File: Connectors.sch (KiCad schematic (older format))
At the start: 4 parts

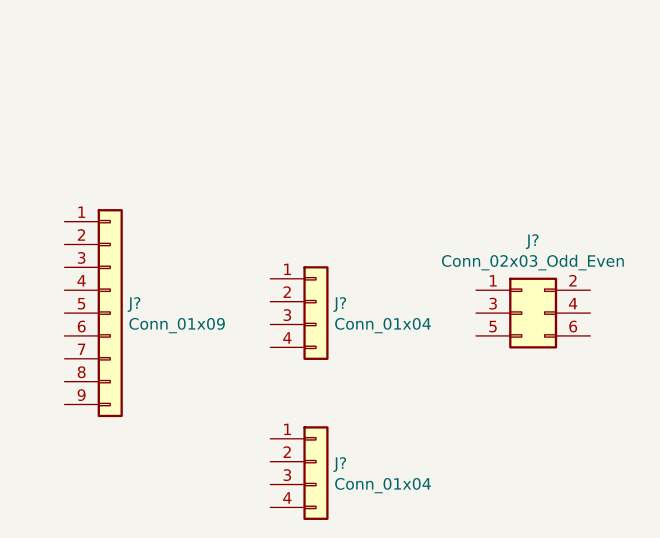
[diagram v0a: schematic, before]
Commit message: Símbolos organizados
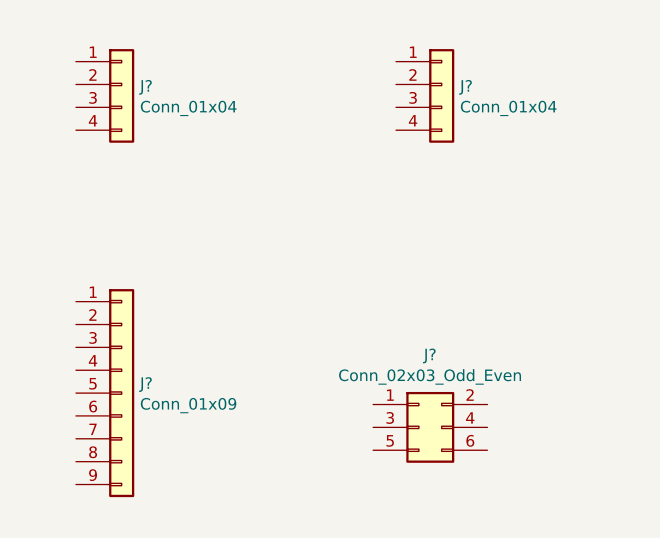
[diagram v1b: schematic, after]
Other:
- moved on the sheet: J?
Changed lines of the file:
@@
 L Connector_Generic:Conn_01x09 J?
 U 1 1 5F03BAF3
-P 5050 3000
-F 0 "J?" H 5130 3042 50  0000 L CNN
-F 1 "Conn_01x09" H 5130 2951 50  0000 L CNN
-F 2 "" H 5050 3000 50  0001 C CNN
-F 3 "~" H 5050 3000 50  0001 C CNN
-	1    5050 3000
+P 5100 3350
+F 0 "J?" H 5180 3392 50  0000 L CNN
+F 1 "Conn_01x09" H 5180 3301 50  0000 L CNN
+F 2 "" H 5100 3350 50  0001 C CNN
+F 3 "~" H 5100 3350 50  0001 C CNN
+	1    5100 3350
 	1    0    0    -1
 $EndComp
@@
 L Connector_Generic:Conn_01x04 J?
 U 1 1 5F03C469
-P 5950 2950
-F 0 "J?" H 6030 2942 50  0000 L CNN
-F 1 "Conn_01x04" H 6030 2851 50  0000 L CNN
-F 2 "" H 5950 2950 50  0001 C CNN
-F 3 "~" H 5950 2950 50  0001 C CNN
-	1    5950 2950
+P 5100 2000
+F 0 "J?" H 5180 1992 50  0000 L CNN
+F 1 "Conn_01x04" H 5180 1901 50  0000 L CNN
+F 2 "" H 5100 2000 50  0001 C CNN
+F 3 "~" H 5100 2000 50  0001 C CNN
+	1    5100 2000
 	1    0    0    -1
 $EndComp
@@
 L Connector_Generic:Conn_02x03_Odd_Even J?
 U 1 1 5F03D0B3
-P 6850 3000
-F 0 "J?" H 6900 3317 50  0000 C CNN
-F 1 "Conn_02x03_Odd_Even" H 6900 3226 50  0000 C CNN
-F 2 "" H 6850 3000 50  0001 C CNN
-F 3 "~" H 6850 3000 50  0001 C CNN
-	1    6850 3000
+P 6400 3500
+F 0 "J?" H 6450 3817 50  0000 C CNN
+F 1 "Conn_02x03_Odd_Even" H 6450 3726 50  0000 C CNN
+F 2 "" H 6400 3500 50  0001 C CNN
+F 3 "~" H 6400 3500 50  0001 C CNN
+	1    6400 3500
 	1    0    0    -1
 $EndComp
@@
 L Connector_Generic:Conn_01x04 J?
 U 1 1 5F03D928
-P 5950 3650
-F 0 "J?" H 6030 3642 50  0000 L CNN
-F 1 "Conn_01x04" H 6030 3551 50  0000 L CNN
-F 2 "" H 5950 3650 50  0001 C CNN
-F 3 "~" H 5950 3650 50  0001 C CNN
-	1    5950 3650
+P 6500 2000
+F 0 "J?" H 6580 1992 50  0000 L CNN
+F 1 "Conn_01x04" H 6580 1901 50  0000 L CNN
+F 2 "" H 6500 2000 50  0001 C CNN
+F 3 "~" H 6500 2000 50  0001 C CNN
+	1    6500 2000
 	1    0    0    -1
 $EndComp

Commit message: Símbolos anotados
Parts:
- gave numbers to parts that had none: 4
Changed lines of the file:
@@
 $EndDescr
 $Comp
-L Connector_Generic:Conn_01x09 J?
+L Connector_Generic:Conn_01x09 J2
 U 1 1 5F03BAF3
 P 5100 3350
-F 0 "J?" H 5180 3392 50  0000 L CNN
+F 0 "J2" H 5180 3392 50  0000 L CNN
 F 1 "Conn_01x09" H 5180 3301 50  0000 L CNN
 F 2 "" H 5100 3350 50  0001 C CNN
@@
 $EndComp
 $Comp
-L Connector_Generic:Conn_01x04 J?
+L Connector_Generic:Conn_01x04 J1
 U 1 1 5F03C469
 P 5100 2000
-F 0 "J?" H 5180 1992 50  0000 L CNN
+F 0 "J1" H 5180 1992 50  0000 L CNN
 F 1 "Conn_01x04" H 5180 1901 50  0000 L CNN
 F 2 "" H 5100 2000 50  0001 C CNN
@@
 $EndComp
 $Comp
-L Connector_Generic:Conn_02x03_Odd_Even J?
+L Connector_Generic:Conn_02x03_Odd_Even J3
 U 1 1 5F03D0B3
 P 6400 3500
-F 0 "J?" H 6450 3817 50  0000 C CNN
+F 0 "J3" H 6450 3817 50  0000 C CNN
 F 1 "Conn_02x03_Odd_Even" H 6450 3726 50  0000 C CNN
 F 2 "" H 6400 3500 50  0001 C CNN
@@
 $EndComp
 $Comp
-L Connector_Generic:Conn_01x04 J?
+L Connector_Generic:Conn_01x04 J4
 U 1 1 5F03D928
 P 6500 2000
-F 0 "J?" H 6580 1992 50  0000 L CNN
+F 0 "J4" H 6580 1992 50  0000 L CNN
 F 1 "Conn_01x04" H 6580 1901 50  0000 L CNN
 F 2 "" H 6500 2000 50  0001 C CNN

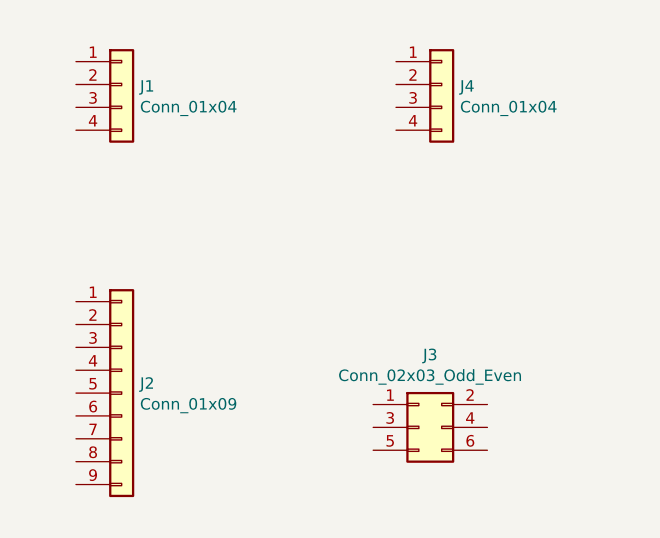
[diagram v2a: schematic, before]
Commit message: Todos os valores e footprints adicionados
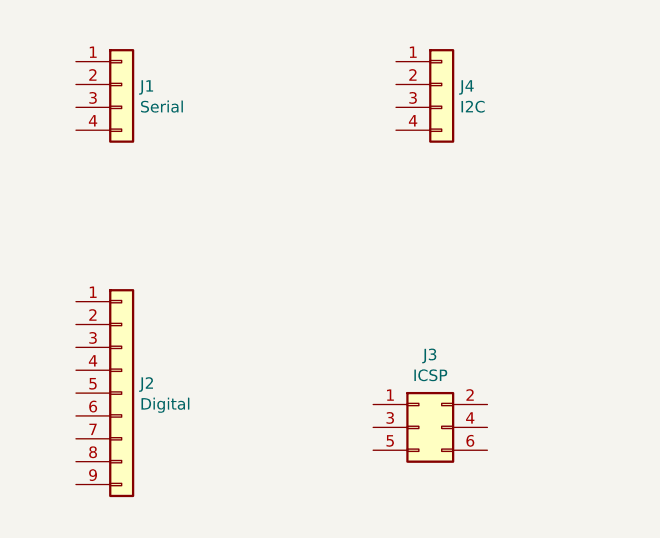
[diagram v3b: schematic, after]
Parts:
- J1: value Conn_01x04 -> Serial; footprint (none) -> Connector_PinHeader_2.54mm:PinHeader_1x04_P2.54mm_Vertical
- J2: value Conn_01x09 -> Digital; footprint (none) -> Connector_PinHeader_2.54mm:PinHeader_1x09_P2.54mm_Vertical
- J3: value Conn_02x03_Odd_Even -> ICSP; footprint (none) -> Connector_PinHeader_2.54mm:PinHeader_2x03_P2.54mm_Vertical
- J4: value Conn_01x04 -> I2C; footprint (none) -> Connector_PinHeader_2.54mm:PinHeader_1x04_P2.54mm_Vertical
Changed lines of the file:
@@
 P 5100 3350
 F 0 "J2" H 5180 3392 50  0000 L CNN
-F 1 "Conn_01x09" H 5180 3301 50  0000 L CNN
-F 2 "" H 5100 3350 50  0001 C CNN
+F 1 "Digital" H 5180 3301 50  0000 L CNN
+F 2 "Connector_PinHeader_2.54mm:PinHeader_1x09_P2.54mm_Vertical" H 5100 3350 50  0001 C CNN
 F 3 "~" H 5100 3350 50  0001 C CNN
 	1    5100 3350
@@
 P 5100 2000
 F 0 "J1" H 5180 1992 50  0000 L CNN
-F 1 "Conn_01x04" H 5180 1901 50  0000 L CNN
-F 2 "" H 5100 2000 50  0001 C CNN
+F 1 "Serial" H 5180 1901 50  0000 L CNN
+F 2 "Connector_PinHeader_2.54mm:PinHeader_1x04_P2.54mm_Vertical" H 5100 2000 50  0001 C CNN
 F 3 "~" H 5100 2000 50  0001 C CNN
 	1    5100 2000
@@
 P 6400 3500
 F 0 "J3" H 6450 3817 50  0000 C CNN
-F 1 "Conn_02x03_Odd_Even" H 6450 3726 50  0000 C CNN
-F 2 "" H 6400 3500 50  0001 C CNN
+F 1 "ICSP" H 6450 3726 50  0000 C CNN
+F 2 "Connector_PinHeader_2.54mm:PinHeader_2x03_P2.54mm_Vertical" H 6400 3500 50  0001 C CNN
 F 3 "~" H 6400 3500 50  0001 C CNN
 	1    6400 3500
@@
 P 6500 2000
 F 0 "J4" H 6580 1992 50  0000 L CNN
-F 1 "Conn_01x04" H 6580 1901 50  0000 L CNN
-F 2 "" H 6500 2000 50  0001 C CNN
+F 1 "I2C" H 6580 1901 50  0000 L CNN
+F 2 "Connector_PinHeader_2.54mm:PinHeader_1x04_P2.54mm_Vertical" H 6500 2000 50  0001 C CNN
 F 3 "~" H 6500 2000 50  0001 C CNN
 	1    6500 2000

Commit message: Ligação dos conectores
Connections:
- net D2: now reaches J2.1 (Pin_1)
- net D3: now reaches J2.2 (Pin_2)
- net D4: now reaches J2.3 (Pin_3)
- net D5: now reaches J2.4 (Pin_4)
- net D6: now reaches J2.5 (Pin_5)
- net D7: now reaches J2.6 (Pin_6)
- net D8: now reaches J2.7 (Pin_7)
- net GND: now reaches J2.8 (Pin_8)
- net GND: now also J1.1 (Pin_1), J3.6 (Pin_6), J4.1 (Pin_1)
- net VCC: now reaches J2.9 (Pin_9)
- net VCC: now also J1.2 (Pin_2), J3.2 (Pin_2), J4.2 (Pin_2)
- net RX: now reaches J1.3 (Pin_3)
- net TX: now reaches J1.4 (Pin_4)
- net MISO: now reaches J3.1 (Pin_1)
- net SCK: now reaches J3.3 (Pin_3)
- net SCK: now also J4.4 (Pin_4)
- net MOSI: now reaches J3.4 (Pin_4)
- net RESET: now reaches J3.5 (Pin_5)
- net SDA: now reaches J4.3 (Pin_3)
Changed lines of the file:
@@
 	1    0    0    -1
 $EndComp
+Text HLabel 6200 3400 0    50   Output ~ 0
+MISO
+Text HLabel 6200 3500 0    50   BiDi ~ 0
+SCK
+Text HLabel 6200 3600 0    50   Output ~ 0
+RESET
+Text HLabel 6700 3400 2    50   Input ~ 0
+VCC
+Text HLabel 6700 3500 2    50   Input ~ 0
+MOSI
+Text HLabel 6700 3600 2    50   Input ~ 0
+GND
+Text HLabel 4900 1900 0    50   Input ~ 0
+GND
+Text HLabel 4900 2000 0    50   Input ~ 0
+VCC
+Text HLabel 4900 2100 0    50   Input ~ 0
+RX
+Text HLabel 4900 2200 0    50   Output ~ 0
+TX
+Text HLabel 6300 1900 0    50   Input ~ 0
+GND
+Text HLabel 6300 2000 0    50   Input ~ 0
+VCC
+Text HLabel 6300 2200 0    50   BiDi ~ 0
+SCK
+Text HLabel 4900 2950 0    50   BiDi ~ 0
+D2
+Text HLabel 4900 3050 0    50   BiDi ~ 0
+D3
+Text HLabel 4900 3150 0    50   BiDi ~ 0
+D4
+Text HLabel 4900 3250 0    50   BiDi ~ 0
+D5
+Text HLabel 4900 3350 0    50   BiDi ~ 0
+D6
+Text HLabel 4900 3450 0    50   BiDi ~ 0
+D7
+Text HLabel 4900 3550 0    50   BiDi ~ 0
+D8
+Text HLabel 4900 3650 0    50   Input ~ 0
+GND
+Text HLabel 4900 3750 0    50   Input ~ 0
+VCC
+Text HLabel 6300 2100 0    50   BiDi ~ 0
+SDA
 $EndSCHEMATC

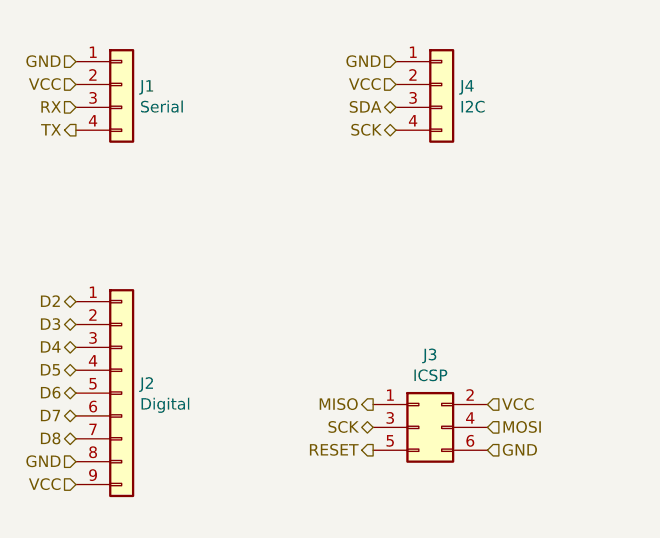
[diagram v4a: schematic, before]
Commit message: Descrições funcionais adicionadas
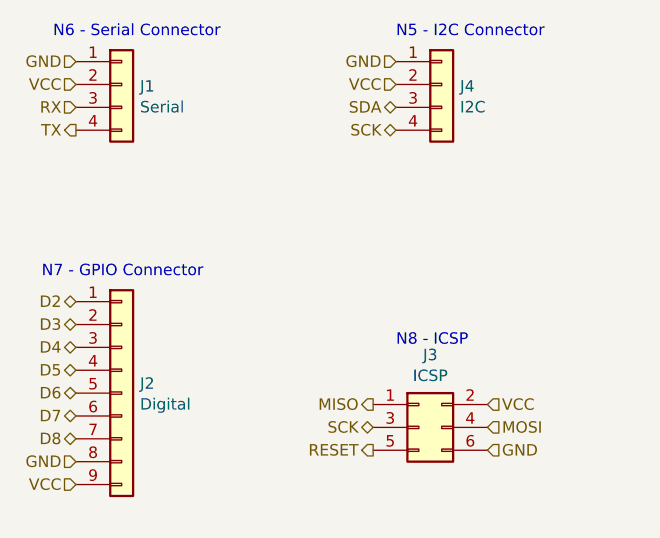
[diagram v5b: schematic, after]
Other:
- note added: "N5 - I2C Connector"
- note added: "N6 - Serial Connector"
- note added: "N7 - GPIO Connector"
- note added: "N8 - ICSP"
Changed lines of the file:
@@
 Text HLabel 6300 2100 0    50   BiDi ~ 0
 SDA
+Text Notes 4800 1800 0    50   ~ 0
+N6 - Serial Connector
+Text Notes 6300 1800 0    50   ~ 0
+N5 - I2C Connector
+Text Notes 4750 2850 0    50   ~ 0
+N7 - GPIO Connector
+Text Notes 6300 3150 0    50   ~ 0
+N8 - ICSP
 $EndSCHEMATC
